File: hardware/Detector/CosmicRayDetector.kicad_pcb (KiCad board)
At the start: 2 copper layers, 88.9 x 78.8 mm, 130 parts, among them J1 USB_B_Micro, J10 Conn_02x02_Odd_Even, J11 Conn_02x02_Odd_Even, J12 Conn_02x02_Odd_Even, J13 Conn_02x02_Odd_Even, J14 Conn_02x02_Odd_Even, J15 Conn_02x02_Odd_Even, J16 Conn_02x02_Odd_Even, J17 Conn_02x02_Odd_Even, J18 Conn_02x20_Counter_Clockwise, J2 Conn_02x02_Odd_Even, J3 Conn_02x02_Odd_Even, J4 Conn_02x02_Odd_Even, J5 Conn_02x02_Odd_Even, J51 Conn_02x05_Counter_Clockwise, J52 Conn_01x04, J6 Conn_02x02_Odd_Even, J7 Conn_02x02_Odd_Even, J8 Conn_02x02_Odd_Even, J9 Conn_02x02_Odd_Even, Q31 BC859, Q32 Q_NMOS_GDS, U1 STM32F030K6Tx, U2 HEF4093B, U3 LCD_I2C, U31 MC34063AD

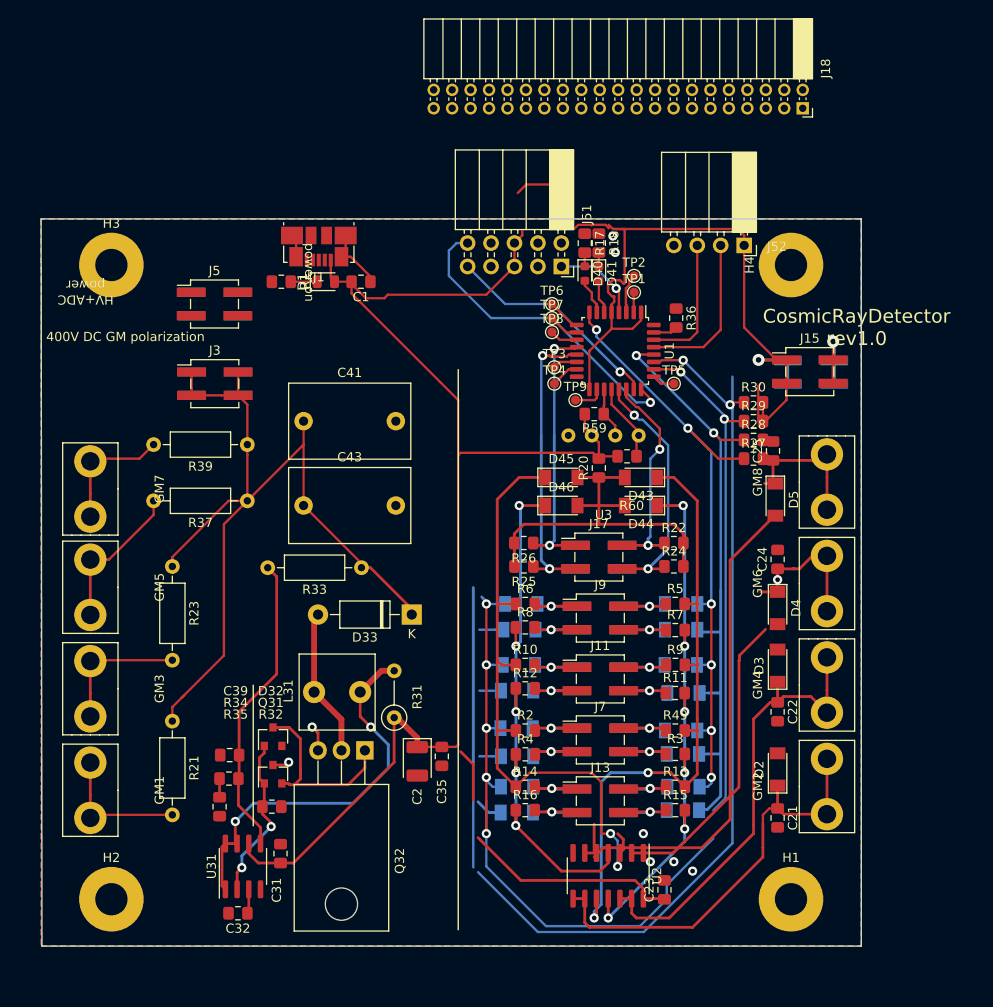
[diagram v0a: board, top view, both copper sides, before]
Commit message: draft of version without expensive connectors
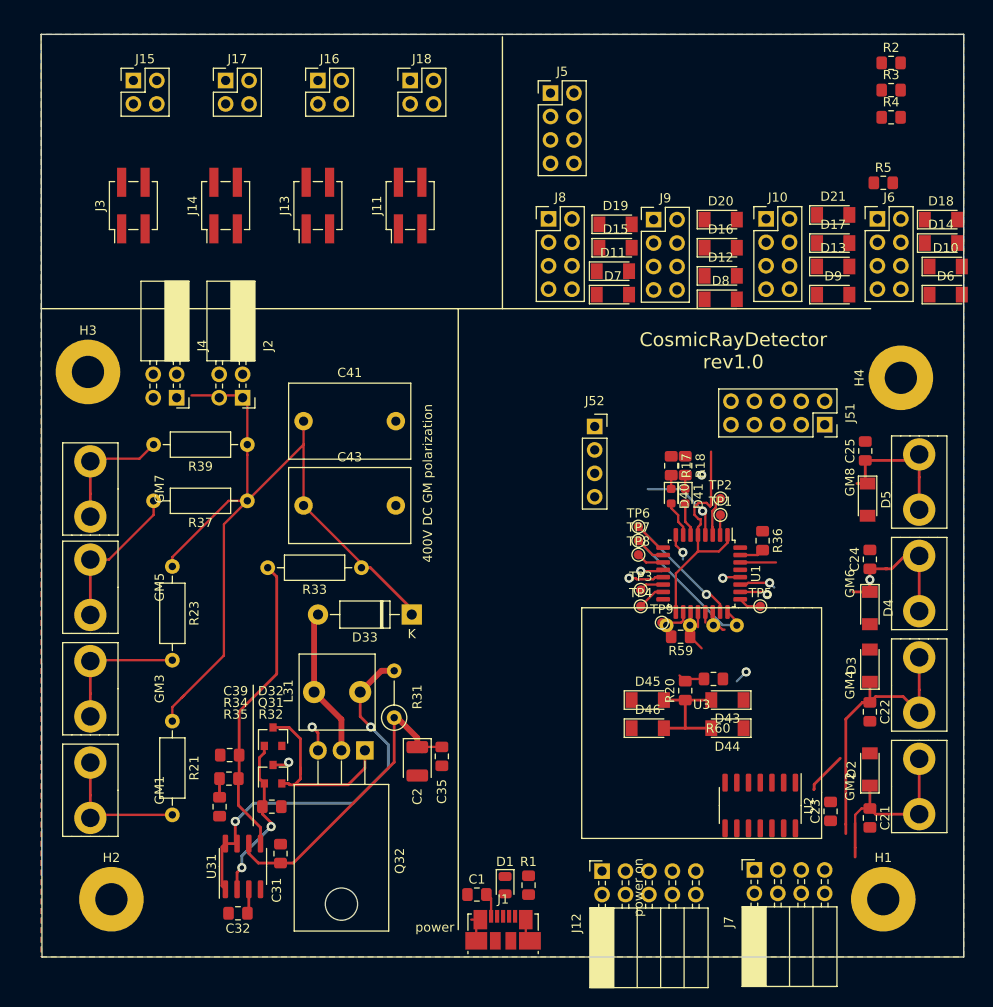
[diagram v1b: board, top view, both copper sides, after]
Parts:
- removed R10, R11, R12, R13, R14, R15, R16, R22, R24, R25, R26, R49, R6, R7, R8, R9: R, Resistor_SMD:R_0805_2012Metric_Pad1.15x1.40mm_HandSolder
- removed R27, R28, R29, R30: 680R, Resistor_SMD:R_0805_2012Metric_Pad1.15x1.40mm_HandSolder
- D10, D11, D12, D13, D14, D15, D16, D17, D18, D19, D20, D21, D6, D7, D8, D9: moved to F.Cu
- J10, J6, J8: value Conn_02x02_Odd_Even -> Conn_02x04_Odd_Even; footprint Connector_PinSocket_2.54mm:PinSocket_2x02_P2.54mm_Vertical_SMD -> Connector_PinHeader_2.54mm:PinHeader_2x04_P2.54mm_Vertical; moved to F.Cu
- J12: value Conn_02x02_Odd_Even -> Conn_02x04_Odd_Even; footprint Connector_PinSocket_2.54mm:PinSocket_2x02_P2.54mm_Vertical_SMD -> Connector_PinSocket_2.54mm:PinSocket_2x05_P2.54mm_Horizontal; moved to F.Cu
- J14: footprint Connector_PinSocket_2.54mm:PinSocket_2x02_P2.54mm_Vertical_SMD -> Connector_PinHeader_2.54mm:PinHeader_2x02_P2.54mm_Vertical_SMD; moved to F.Cu
- J15, J17: footprint Connector_PinHeader_2.54mm:PinHeader_2x02_P2.54mm_Vertical_SMD -> Connector_PinHeader_2.54mm:PinHeader_2x02_P2.54mm_Vertical
- J16: footprint Connector_PinSocket_2.54mm:PinSocket_2x02_P2.54mm_Vertical_SMD -> Connector_PinHeader_2.54mm:PinHeader_2x02_P2.54mm_Vertical; moved to F.Cu
- J18: value Conn_02x20_Counter_Clockwise -> Conn_02x02_Odd_Even; footprint Connector_PinSocket_2.00mm:PinSocket_2x21_P2.00mm_Horizontal -> Connector_PinHeader_2.54mm:PinHeader_2x02_P2.54mm_Vertical
- J2, J4: footprint Connector_PinSocket_2.54mm:PinSocket_2x02_P2.54mm_Vertical_SMD -> Connector_PinSocket_2.54mm:PinSocket_2x02_P2.54mm_Horizontal; moved to F.Cu
- J5, J9: value Conn_02x02_Odd_Even -> Conn_02x04_Odd_Even; footprint Connector_PinHeader_2.54mm:PinHeader_2x02_P2.54mm_Vertical_SMD -> Connector_PinHeader_2.54mm:PinHeader_2x04_P2.54mm_Vertical
- J51: footprint Connector_PinSocket_2.54mm:PinSocket_2x05_P2.54mm_Horizontal -> Connector_PinSocket_2.54mm:PinSocket_2x05_P2.54mm_Vertical
- J52: footprint Connector_PinSocket_2.54mm:PinSocket_1x04_P2.54mm_Horizontal -> Connector_PinSocket_2.54mm:PinSocket_1x04_P2.54mm_Vertical
- J7: value Conn_02x02_Odd_Even -> Conn_02x04_Odd_Even; footprint Connector_PinHeader_2.54mm:PinHeader_2x02_P2.54mm_Vertical_SMD -> Connector_PinSocket_2.54mm:PinSocket_2x04_P2.54mm_Horizontal
- R2, R3, R4, R5: value R -> 680R
- moved R2 82.5 mm to (92.1, -11.9)
- moved J15 79.8 mm to (10.0, -10.0)
- moved R4 79.6 mm to (92.1, -6.01)
- moved J1 76.7 mm to (50.1, 82.1), turned to 0 degrees
- moved R3 75.7 mm to (92.1, -8.96)
- moved D18 74.1 mm to (97.5, 5.08), turned to 0 degrees
- moved D21 73.3 mm to (85.9, 4.57), turned to 0 degrees
- moved J13 71.4 mm to (30.0, 3.56), turned to 90 degrees
- moved R1 70.7 mm to (52.8, 77.2), turned to 270 degrees
- moved D14 69.9 mm to (97.5, 7.62), turned to 0 degrees
- moved D1 68.2 mm to (50.3, 77.2), turned to 270 degrees
- moved D17 68.2 mm to (85.9, 7.62), turned to 0 degrees
- moved C1 67.6 mm to (47.2, 78.2), turned to 0 degrees
- moved J14 66.0 mm to (20.0, 3.56), turned to 90 degrees
- moved J17 65.6 mm to (20.0, -10.0)
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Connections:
- D10 pad 2: COL1 -> /BoardConnector/COL1_LOCAL
- D11 pad 2: COL1 -> /BoardConnector/COL1_LOCAL
- D12 pad 2: COL1 -> /BoardConnector/COL1_LOCAL
- D13 pad 2: COL1 -> /BoardConnector/COL1_LOCAL
- D14 pad 2: COL2 -> /BoardConnector/COL2_LOCAL
- D15 pad 2: COL2 -> /BoardConnector/COL2_LOCAL
- D16 pad 2: COL2 -> /BoardConnector/COL2_LOCAL
- D17 pad 2: COL2 -> /BoardConnector/COL2_LOCAL
- D18 pad 2: COL3 -> /BoardConnector/COL3_LOCAL
- D19 pad 2: COL3 -> /BoardConnector/COL3_LOCAL
- D20 pad 2: COL3 -> /BoardConnector/COL3_LOCAL
- D21 pad 2: COL3 -> /BoardConnector/COL3_LOCAL
- D6 pad 2: COL0 -> /BoardConnector/COL0_LOCAL
- D7 pad 2: COL0 -> /BoardConnector/COL0_LOCAL
- D8 pad 2: COL0 -> /BoardConnector/COL0_LOCAL
- D9 pad 2: COL0 -> /BoardConnector/COL0_LOCAL
- J10 pad 1: INT23 -> GND
- J10 pad 2: INT21 -> INT34
- J10 pad 3: INT24 -> GND
- J10 pad 4: INT22 -> INT33
- J11 pad 1: INT23 -> GM_LAMP_POLARIZATION
- J11 pad 2: INT21 -> GM_LAMP_POLARIZATION
- J11 pad 3: INT24 -> GM_LAMP_POLARIZATION
- J11 pad 4: INT22 -> GM_LAMP_POLARIZATION
- J12 pad 1: INT33 -> /BoardConnector/COL0_LOCAL
- J12 pad 2: INT31 -> /BoardConnector/ROW0_LOCAL
- J12 pad 3: INT34 -> /BoardConnector/COL1_LOCAL
- J12 pad 4: INT32 -> /BoardConnector/ROW1_LOCAL
- J13 pad 1: INT33 -> GM_LAMP_POLARIZATION
- J13 pad 2: INT31 -> GM_LAMP_POLARIZATION
- J13 pad 3: INT34 -> GM_LAMP_POLARIZATION
- J13 pad 4: INT32 -> GM_LAMP_POLARIZATION
- J14 pad 1: VCC_5V -> GM_LAMP_POLARIZATION
- J14 pad 2: GND -> GM_LAMP_POLARIZATION
- J14 pad 3: VCC_5V -> GM_LAMP_POLARIZATION
- J14 pad 4: GND -> GM_LAMP_POLARIZATION
- J15 pad 1: VCC_5V -> GND
- J15 pad 3: VCC_5V -> GND
- J16 pad 1: ROW3 -> GND
- J16 pad 2: ROW0 -> GND
- J16 pad 3: ROW2 -> GND
- J16 pad 4: ROW1 -> GND
- J17 pad 1: ROW3 -> GND
- J17 pad 2: ROW0 -> GND
- J17 pad 3: ROW2 -> GND
- J17 pad 4: ROW1 -> GND
- J18 pad 1: (no net) -> GND
- J18 pad 2: (no net) -> GND
- J18 pad 3: (no net) -> GND
- J18 pad 4: (no net) -> GND
- J5 pad 1: GND -> COL0
- J5 pad 2: GND -> ROW0
- J5 pad 3: GND -> COL1
- J5 pad 4: GND -> ROW1
- J6 pad 1: INT03 -> GND
- J6 pad 2: INT01 -> INT04
- J6 pad 3: INT04 -> GND
- J6 pad 4: INT02 -> INT03
- J7 pad 1: INT03 -> GND
- J7 pad 2: INT01 -> GM4
- J7 pad 3: INT04 -> GND
- J7 pad 4: INT02 -> GM3
- J8 pad 1: INT13 -> GND
- J8 pad 2: INT11 -> INT14
- J8 pad 3: INT14 -> GND
- J8 pad 4: INT12 -> INT13
- J9 pad 1: INT13 -> GND
- J9 pad 2: INT11 -> INT24
- J9 pad 3: INT14 -> GND
- J9 pad 4: INT12 -> INT23
- R2 pad 1: GM3 -> /BoardConnector/COL0_LOCAL
- R2 pad 2: INT03 -> VCC_5V
- R3 pad 1: INT02 -> /BoardConnector/COL1_LOCAL
- R3 pad 2: GM2 -> VCC_5V
- R4 pad 1: GM4 -> /BoardConnector/COL2_LOCAL
- R4 pad 2: INT04 -> VCC_5V
- R5 pad 1: INT11 -> /BoardConnector/COL3_LOCAL
- R5 pad 2: GM1 -> VCC_5V
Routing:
- net VCC_5V: track 264.5 -> 65.3 mm, vias 1 -> 0
- net COL3: track 138.8 -> 3.97 mm, vias 2 -> 1
- net COL2: track 128.1 -> 3.10 mm, vias 7 -> 1
- net GM1: track 68.4 -> 0.00 mm, vias 2 -> 0
- net GM3: track 67.8 -> 0.00 mm, vias 2 -> 0
- net COL0: track 70.2 -> 2.97 mm, vias 6 -> 1
- net COL1: track 67.3 -> 1.93 mm, vias 2 -> 1
- net GM2: track 64.5 -> 0.00 mm, vias 6 -> 0
- net GM4: track 60.3 -> 0.00 mm, vias 5 -> 0
- net Net-(C25-Pad1): track 70.4 -> 15.4 mm
- net Net-(D43-Pad2): track 40.6 -> 12.3 mm
- net Net-(C24-Pad1): track 49.2 -> 21.0 mm
- net ROW2: track 32.1 -> 4.05 mm, vias 2 -> 1
- net Net-(C21-Pad1): track 46.6 -> 20.0 mm
- net ROW1: track 27.5 -> 1.14 mm, vias 2 -> 0
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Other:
- board size 88.9 x 78.8 mm -> 100 x 100 mm
- board text added: "power"
- board text removed: "HV+ADC power"
